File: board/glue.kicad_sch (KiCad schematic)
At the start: 25 parts, among them J1 Conn_01x05_Pin, J8 SD_Card_Receptacle, U12 GLUE, U13 SN74LVC245APW, U14 LD1117V33

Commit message: checkpoint
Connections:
- net A1: now also U12.51 (I/O); no longer U12.52 (I/O)
- net A16: now also U12.41 (I/O); no longer U12.56 (I/O)
- net A17: now also U12.39 (I/O); no longer U12.57 (I/O)
- net A18: now also U12.40 (I/O); no longer U12.58 (I/O)
- net A19: now also U12.35 (I/O); no longer U12.60 (I/O)
- net A2: now also U12.55 (I/O); no longer U12.51 (I/O)
- net A20: now also U12.33 (I/O); no longer U12.9 (I/O)
- net A21: now also U12.56 (I/O); no longer U12.10 (I/O)
- net A22: now also U12.57 (I/O); no longer U12.11 (I/O)
- net A23: now also U12.31 (I/O); no longer U12.12 (I/O/PD1)
- net BOOT_BEEP: now also U12.70 (I/O); no longer U12.48 (I/O)
- net CPST_START_FIELD: now also U12.1 (INPUT/GCLR); no longer U12.69 (I/O)
- net D0: now also U12.61 (I/O); no longer U12.73 (I/O)
- net D1: now also U12.27 (I/O); no longer U12.74 (I/O)
- net D2: now also U12.63 (I/O); no longer U12.75 (I/O)
- net D3: now also U12.24 (I/O); no longer U12.76 (I/O)
- net D4: now also U12.65 (I/O); no longer U12.77 (I/O)
- net D5: now also U12.22 (I/O); no longer U12.79 (I/O)
- net D6: now also U12.64 (I/O); no longer U12.80 (I/O)
- net D7: now also U12.25 (I/O); no longer U12.81 (I/O/GCLK3)
- net DBGHILED_LE: now also U12.69 (I/O); no longer U12.46 (I/O)
- net DBGLOLED_LE: now also U12.68 (I/O); no longer U12.45 (I/O/PD2)
- net DEBUG_IN: now also U12.83 (INPUT/GCLK1); no longer U12.1 (INPUT/GCLR)
- net DEBUG_OUT: now also U12.67 (I/O); no longer U12.44 (I/O)
- net R/~{W}: now also U12.58 (I/O); no longer U12.6 (I/O)
- net SD_3V3OE: now also U12.80 (I/O); no longer U12.67 (I/O)
- net SD_CS_5V: now also U12.81 (I/O/GCLK3); no longer U12.68 (I/O)
- net SPI_DI_5V: now also U12.77 (I/O); no longer U12.64 (I/O)
- net SPI_DO_3V3: now also U12.76 (I/O); no longer U12.63 (I/O)
- net SPI_SCK_5V: now also U12.79 (I/O); no longer U12.65 (I/O)
- net SYSCLK: now also U12.34 (I/O); no longer U12.83 (INPUT/GCLK1)
- net VIDEO_PRESENT: now also U12.2 (INPUT/OE2/GCLK2); no longer U12.55 (I/O)
- net ~{AS}: now also U12.60 (I/O); no longer U12.8 (I/O)
- net ~{BERR}: now also U12.44 (I/O); no longer U12.34 (I/O)
- net ~{CPST_SELECT}: now also U12.74 (I/O); no longer U12.61 (I/O)
- net ~{DTACK}: now also U12.30 (I/O); no longer U12.33 (I/O)
- net ~{FC0}: now also U12.52 (I/O); no longer U12.39 (I/O)
- net ~{FC1}: now also U12.49 (I/O); no longer U12.40 (I/O)
- net ~{FC2}: now also U12.50 (I/O); no longer U12.41 (I/O)
- net ~{HALT}: now also U12.36 (I/O); no longer U12.50 (I/O)
- net ~{IO_DTACK}: now also U12.16 (I/O); no longer U12.27 (I/O)
- net ~{IO_IACK}: now also U12.21 (I/O); no longer U12.31 (I/O)
- net ~{IO_IRQ}: now also U12.18 (I/O); no longer U12.29 (I/O)
- net ~{IO_SELECT}: now also U12.12 (I/O/PD1); no longer U12.24 (I/O)
- net ~{IPL0}: now also U12.48 (I/O); no longer U12.35 (I/O)
- net ~{IPL1}: now also U12.45 (I/O/PD2); no longer U12.36 (I/O)
- net ~{IPL2}: now also U12.46 (I/O); no longer U12.37 (I/O)
- net ~{LDS}: now also U12.29 (I/O); no longer U12.4 (I/O)
- net ~{RAM_SELECT_1}: now also U12.5 (I/O); no longer U12.16 (I/O)
- net ~{RAM_SELECT_2}: now also U12.6 (I/O); no longer U12.17 (I/O)
- net ~{RAM_SELECT_3}: now also U12.8 (I/O); no longer U12.18 (I/O)
- net ~{RAM_SELECT_4}: now also U12.9 (I/O); no longer U12.20 (I/O)
- net ~{RESET}: now also U12.37 (I/O); no longer U12.2 (INPUT/OE2/GCLK2)
- net ~{ROM_SELECT}: now also U12.4 (I/O); no longer U12.15 (I/O)
- net ~{R}/W: now also U12.73 (I/O); no longer U12.49 (I/O)
- net ~{UDS}: now also U12.28 (I/O); no longer U12.5 (I/O)
- net ~{VIDEO_DTACK}: now also U12.17 (I/O); no longer U12.28 (I/O)
- net ~{VIDEO_IACK}: now also U12.75 (I/O); no longer U12.70 (I/O)
- net ~{VIDEO_IRQ}: now also U12.20 (I/O); no longer U12.30 (I/O)
- net ~{VIDEO_SELECT}: now also U12.15 (I/O); no longer U12.25 (I/O)
- net ~{WRITE_HI}: now also U12.11 (I/O); no longer U12.22 (I/O)
- net ~{WRITE_LO}: now also U12.10 (I/O); no longer U12.21 (I/O)
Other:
- moved on the sheet: R17, R18, R19, R56

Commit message: checkpoint before deleting composite video
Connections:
- net CPST_START_FIELD renamed OBVID_FRAME
- net CPST_TDI renamed OBVID_TDI
- net ~{CPST_DTACK} renamed ~{OBVID_DTACK}
- net ~{CPST_SELECT} renamed ~{OBVID_SELECT}
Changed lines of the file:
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@@
 		)
 	)
-	(global_label "~{CPST_DTACK}"
+	(global_label "~{OBVID_DTACK}"
 		(shape input)
 		(at 59.69 168.91 180)
@@
 		)
 	)
-	(global_label "CPST_TDI"
+	(global_label "OBVID_TDI"
 		(shape output)
 		(at 102.87 166.37 0)
@@
 		)
 	)
-	(global_label "~{CPST_SELECT}"
+	(global_label "~{OBVID_SELECT}"
 		(shape output)
 		(at 102.87 140.97 0)
@@
 		)
 	)
-	(global_label "CPST_START_FIELD"
+	(global_label "OBVID_FRAME"
 		(shape input)
 		(at 57.15 161.29 180)

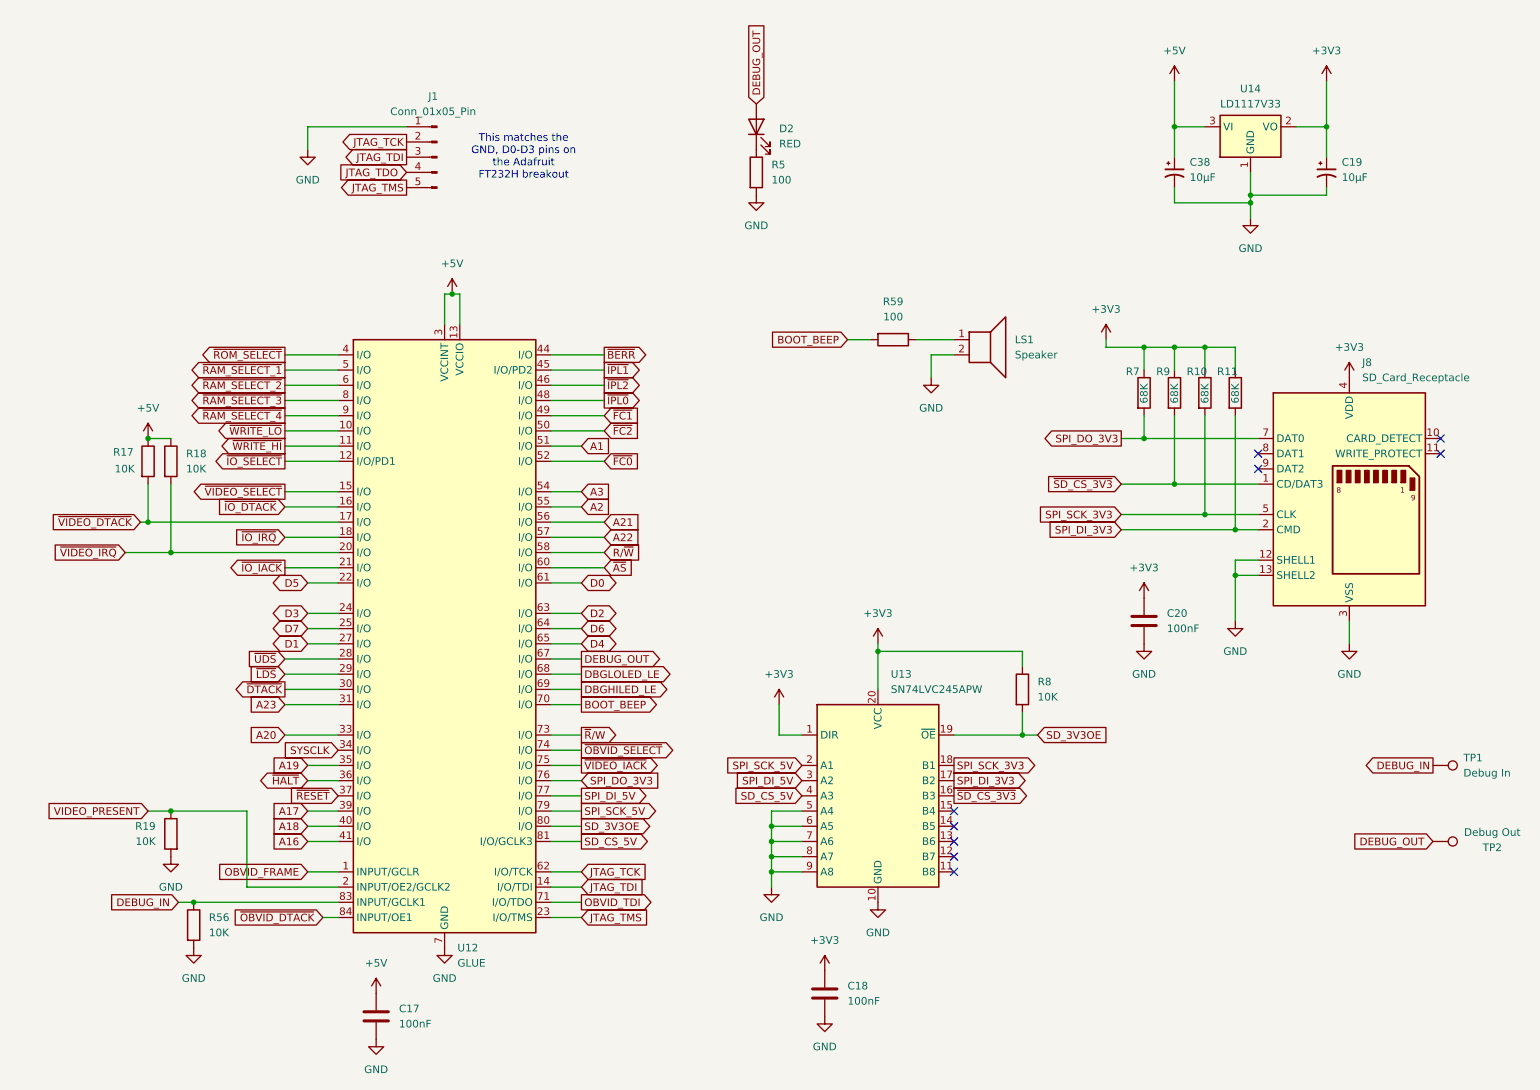
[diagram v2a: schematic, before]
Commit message: CF card, composite, VGA
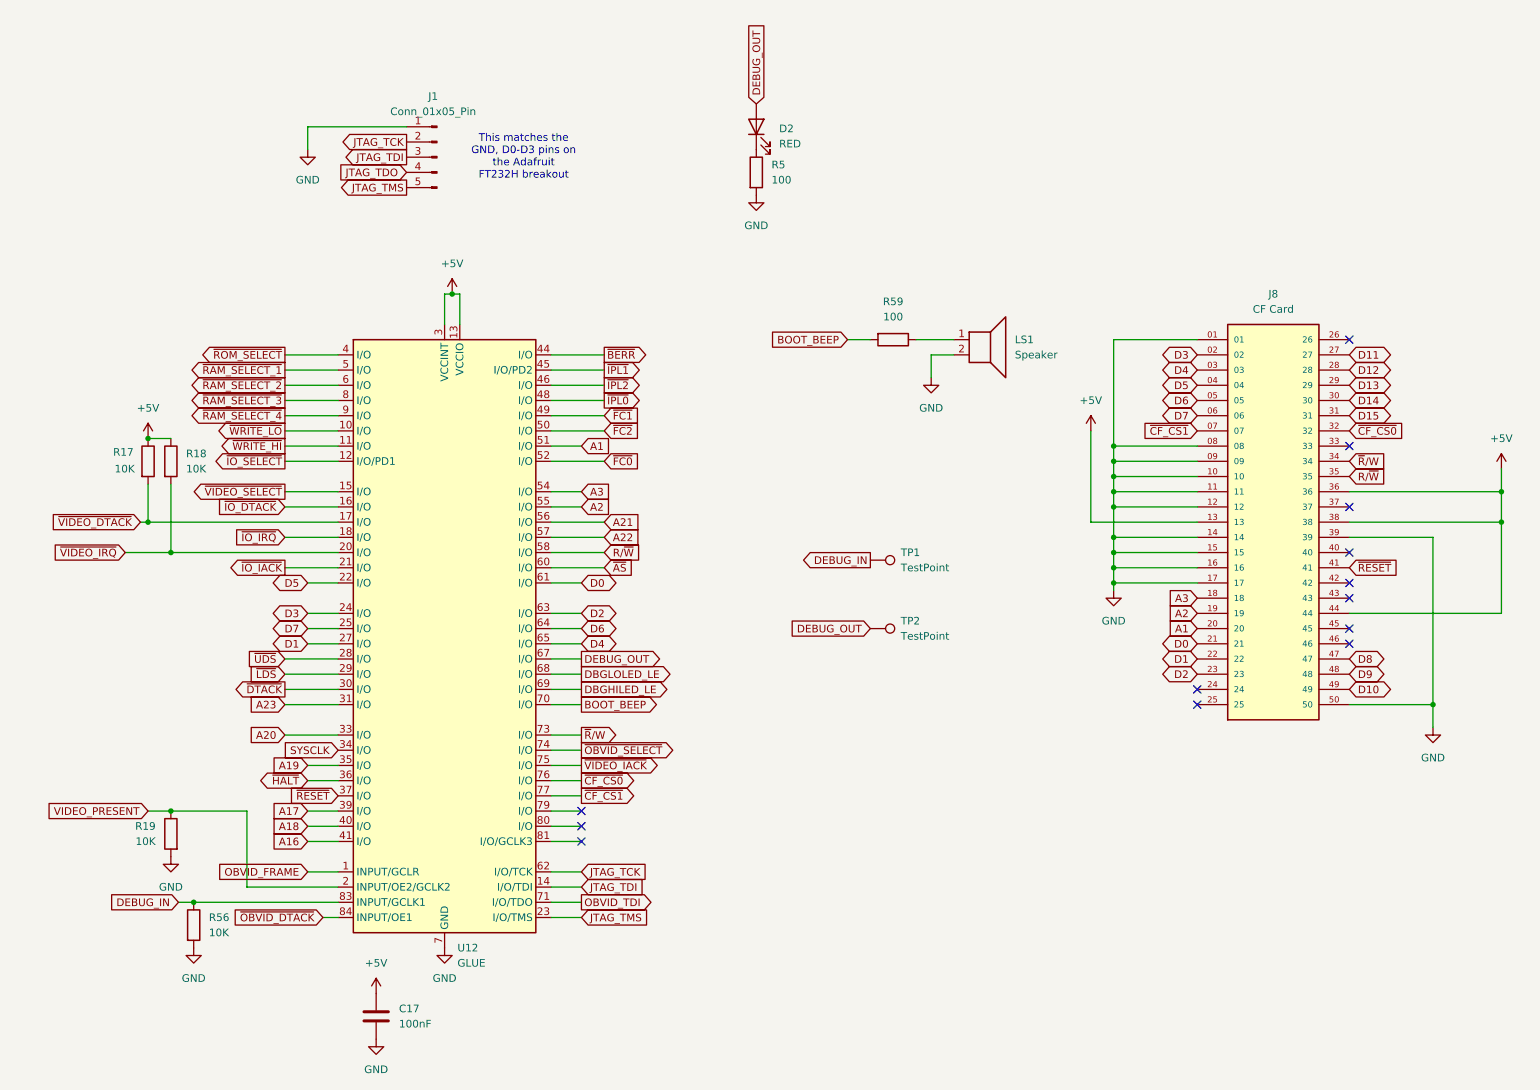
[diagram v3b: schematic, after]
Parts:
- removed C18, C20: 100nF, Capacitor_THT:C_Disc_D5.0mm_W2.5mm_P5.00mm, symbol Device:C
- removed C19, C38: 10µF, Capacitor_THT:CP_Radial_D5.0mm_P2.50mm, symbol Device:C_Polarized_Small_US
- removed J8: SD_Card_Receptacle, board:10067847-001RLF, symbol Connector:SD_Card_Receptacle
- removed R10, R11, R7, R9: 68K, Resistor_THT:R_Axial_DIN0207_L6.3mm_D2.5mm_P10.16mm_Horizontal, symbol Device:R
- removed R8: 10K, Resistor_THT:R_Axial_DIN0207_L6.3mm_D2.5mm_P10.16mm_Horizontal, symbol Device:R
- removed U13: SN74LVC245APW, Package_DIP:DIP-20_W7.62mm, symbol Logic_LevelTranslator:SN74LVC245APW
- removed U14: LD1117V33, Package_TO_SOT_THT:TO-220-3_Vertical, symbol Regulator_Linear:LD1117V33
- added J8: CF Card, board:SAMTEC_CFT-125-01-L-D-RA-01-SL, symbol SAMTEC:CFT-125-01-L-D-RA-01-SL
- TP1: value Debug In -> TestPoint
- TP2: value Debug Out -> TestPoint
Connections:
- net +5V: now also J8.13, J8.36, J8.38, J8.44
- net A1: now also J8.20
- net A2: now also J8.19
- net A3: now also J8.18
- net D0: now also J8.21
- net D1: now also J8.22
- net D2: now also J8.23
- net D3: now also J8.02
- net D4: now also J8.03
- net D5: now also J8.04
- net D6: now also J8.05
- net D7: now also J8.06
- net GND: now also J8.01, J8.08, J8.09, J8.10, J8.11, J8.12, J8.14, J8.15, J8.16, J8.17, J8.39, J8.50
- net R/~{W}: now also J8.35
- net ~{RESET}: now also J8.41
- net ~{R}/W: now also J8.34
- net SD_3V3OE: no longer names the net of U12.80 (I/O)
- net SD_CS_5V: no longer names the net of U12.81 (I/O/GCLK3)
- net SPI_DI_5V renamed ~{CF_CS1}
- net ~{CF_CS1}: now also J8.07
- net SPI_DO_3V3 renamed ~{CF_CS0}
- net ~{CF_CS0}: now also J8.32
- net SPI_SCK_5V: no longer names the net of U12.79 (I/O)
- new net D10: J8.49
- new net D11: J8.27
- new net D12: J8.28
- new net D13: J8.29
- new net D14: J8.30
- new net D15: J8.31
- new net D8: J8.47
- new net D9: J8.48
- no-connect marks 9 -> 13

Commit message: checkpoint
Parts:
- removed LS1: Speaker, Buzzer_Beeper:MagneticBuzzer_StarMicronics_QMX, symbol Device:Speaker
- removed R17, R18: 10K, Resistor_THT:R_Axial_DIN0207_L6.3mm_D2.5mm_P10.16mm_Horizontal, symbol Device:R
- removed R59: 100, Resistor_THT:R_Axial_DIN0207_L6.3mm_D2.5mm_P10.16mm_Horizontal, symbol Device:R
- removed TP1, TP2: TestPoint, Connector_PinHeader_2.54mm:PinHeader_1x01_P2.54mm_Vertical, symbol Connector:TestPoint
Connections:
- net GND: now also J8.S1, J8.S2, J8.S3, J8.S4
- net A4: now reaches U12.79 (I/O)
- net A5: now reaches U12.80 (I/O)
- net A6: now reaches U12.81 (I/O/GCLK3)
- net A16 renamed ENGINE_TDO
- net A17 renamed ENGINE_TCK
- net A18 renamed ENGINE_TDI
- net BOOT_BEEP renamed ENGINE_TMS
- net D10: no longer names the net of J8.49
- net D11: no longer names the net of J8.27
- net D12: no longer names the net of J8.28
- net D13: no longer names the net of J8.29
- net D14: no longer names the net of J8.30
- net D15: no longer names the net of J8.31
- net D8: no longer names the net of J8.47
- net D9: no longer names the net of J8.48
- net DBGHILED_LE renamed IO_RESET
- net DBGLOLED_LE renamed AUDIO_LE
- net OBVID_FRAME renamed ~{OBVID_IRQ}
- net SYSCLK renamed CPUCLK
- net VIDEO_PRESENT: no longer names the net of R19.1, U12.2 (INPUT/OE2/GCLK2)
- net ~{FC0} renamed FC0
- net ~{FC1} renamed FC1
- net ~{FC2} renamed FC2
- net ~{IO_DTACK} renamed ~{IO_DTACK_MISO}
- net ~{IO_IACK} renamed ~{IO_IACK_SCK}
- net ~{IO_SELECT} renamed ~{IO_SELECT_MOSI}
- net ~{OBVID_DTACK} renamed OBVID_STALL
- net ~{VIDEO_DTACK} renamed ~{ENGINE_DTACK}
- net ~{VIDEO_IACK} renamed ~{ENGINE_IACK}
- net ~{VIDEO_IRQ} renamed ~{ENGINE_IRQ}
- net ~{VIDEO_SELECT} renamed ~{ENGINE_SELECT}
- no-connect marks 13 -> 18
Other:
- moved on the sheet: C17, R19, R56, U12

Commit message: Board rev1 PCB complete, already have a spot fix
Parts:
- removed J8: CF Card, board:SAMTEC_CFT-125-01-L-D-RA-01-SL, symbol SAMTEC:CFT-125-01-L-D-RA-01-SL
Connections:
- no-connect marks 18 -> 0
